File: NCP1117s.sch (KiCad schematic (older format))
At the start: 16 parts, among them U18 NCP1117ST33T3G, U19 AP2120N-1.8TRG1

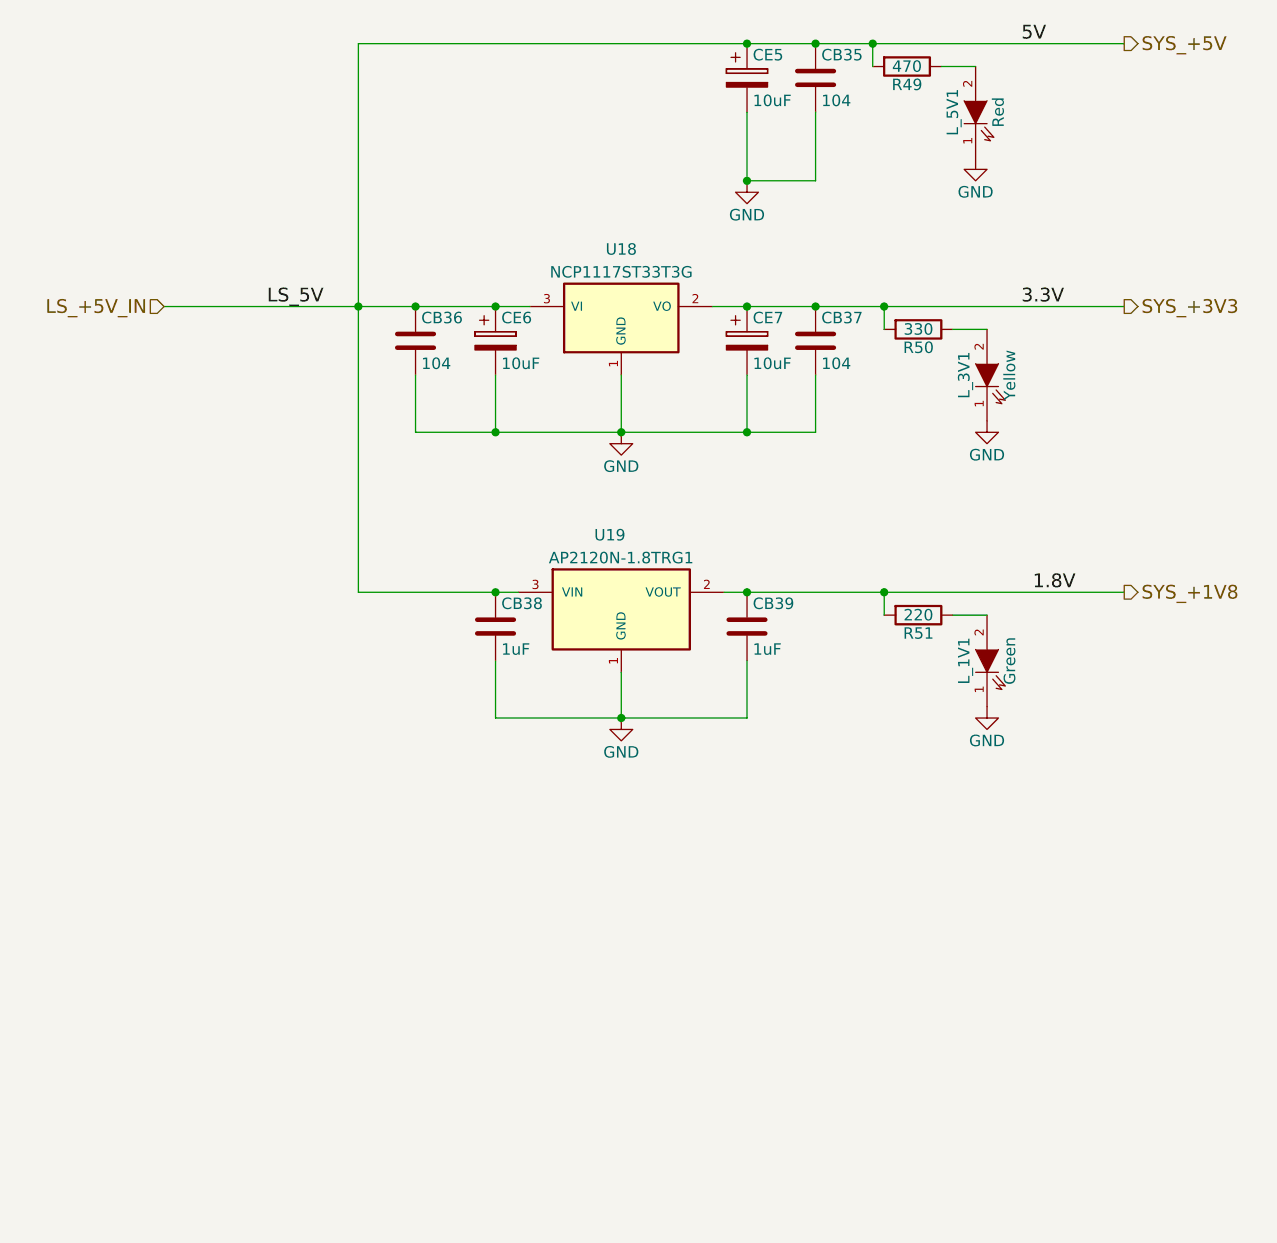
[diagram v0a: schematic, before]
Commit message: Improved the pin comatibility to match with other ardupilot project.
Signed-off-by: Akira Tsukamoto <akira-t@s9.dion.ne.jp>
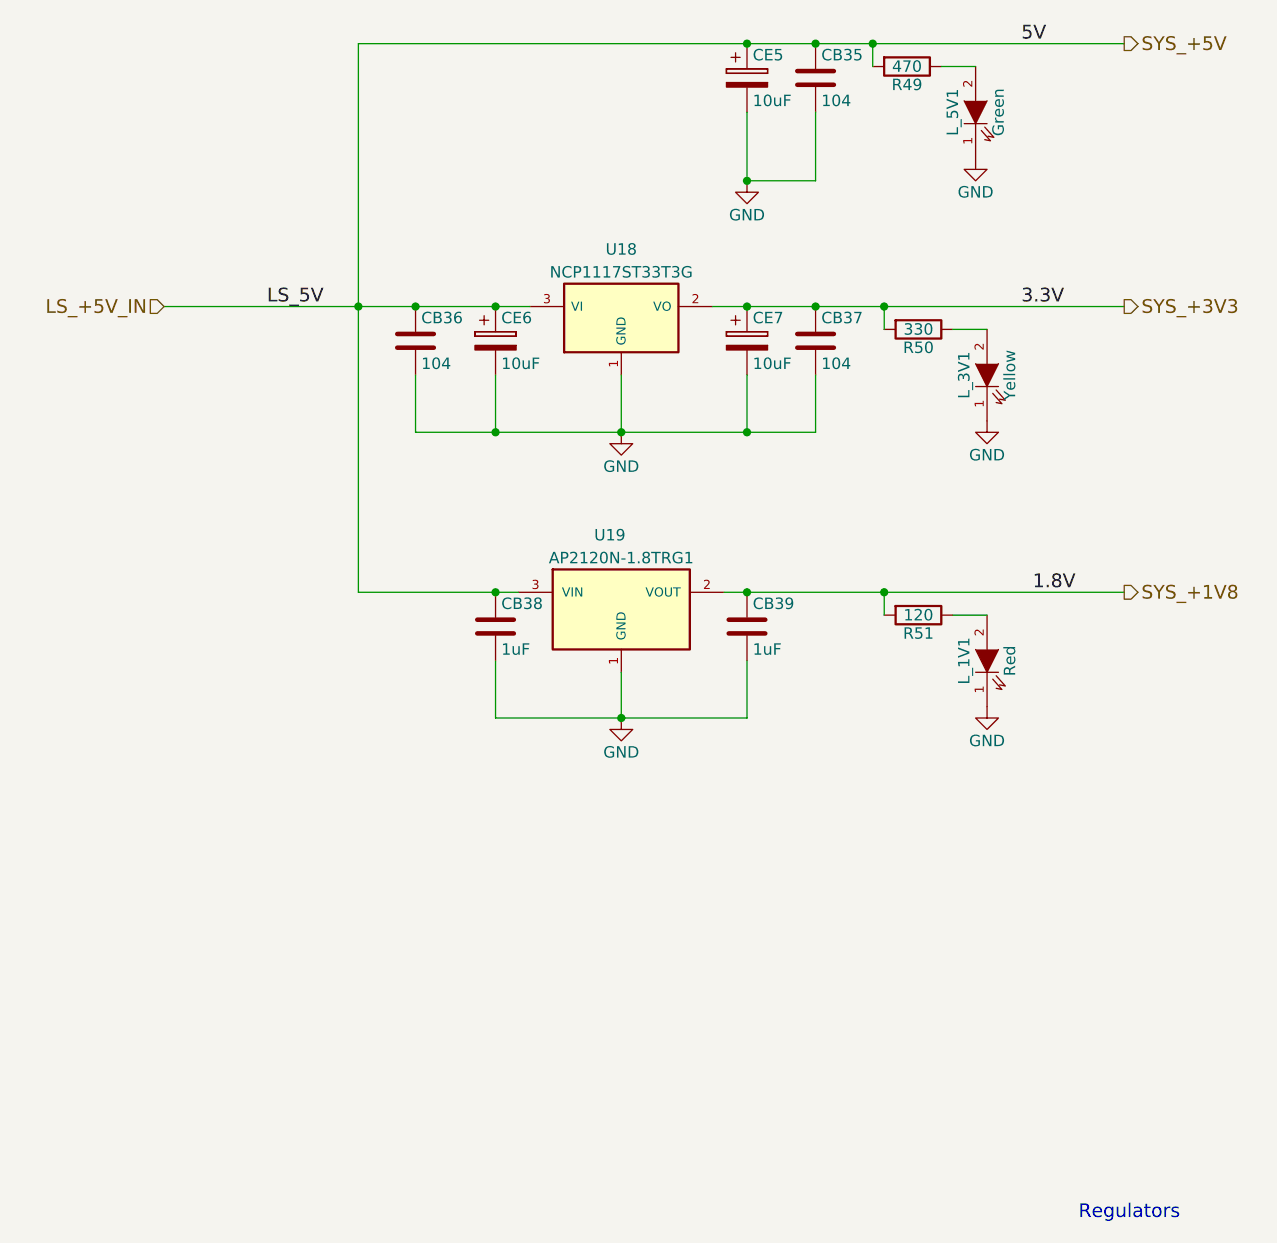
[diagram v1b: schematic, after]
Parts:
- L_1V1: value Green -> Red
- L_5V1: value Red -> Green
- R51: value 220 -> 120
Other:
- note added: "Regulators"
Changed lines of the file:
@@
 $EndDescr
 $Comp
-L GND #PWR094
+L GND #PWR096
 U 1 1 5707ADD4
 P 5300 4050
-F 0 "#PWR094" H 5300 3800 50  0001 C CNN
+F 0 "#PWR096" H 5300 3800 50  0001 C CNN
 F 1 "GND" H 5300 3900 50  0000 C CNN
 F 2 "" H 5300 4050 60  0000 C CNN
@@
 $EndComp
 $Comp
-L GND #PWR095
+L GND #PWR097
 U 1 1 5707AE00
 P 5300 5300
-F 0 "#PWR095" H 5300 5050 50  0001 C CNN
+F 0 "#PWR097" H 5300 5050 50  0001 C CNN
 F 1 "GND" H 5300 5150 50  0000 C CNN
 F 2 "" H 5300 5300 60  0000 C CNN
@@
 $EndComp
 $Comp
-L GND #PWR096
+L GND #PWR098
 U 1 1 5767AC24
 P 6900 4000
-F 0 "#PWR096" H 6900 3750 50  0001 C CNN
+F 0 "#PWR098" H 6900 3750 50  0001 C CNN
 F 1 "GND" H 6900 3850 50  0000 C CNN
 F 2 "" H 6900 4000 60  0000 C CNN
@@
 P 6600 4850
 F 0 "R51" V 6680 4850 50  0000 C CNN
-F 1 "220" V 6600 4850 50  0000 C CNN
+F 1 "120" V 6600 4850 50  0000 C CNN
 F 2 "droneworks:R_0603_Hand_droneworks" V 6530 4850 50  0001 C CNN
 F 3 "" H 6600 4850 50  0000 C CNN
@@
 P 6900 5050
 F 0 "L_1V1" H 6900 5150 50  0000 C CNN
-F 1 "Green" H 6900 4950 50  0000 C CNN
+F 1 "Red" H 6900 4950 50  0000 C CNN
 F 2 "droneworks:LED_0603_1608mm_droneworks" H 6900 5050 50  0001 C CNN
 F 3 "" H 6900 5050 50  0000 C CNN
@@
 $EndComp
 $Comp
-L GND #PWR097
+L GND #PWR099
 U 1 1 5767AE4A
 P 6900 5250
-F 0 "#PWR097" H 6900 5000 50  0001 C CNN
+F 0 "#PWR099" H 6900 5000 50  0001 C CNN
 F 1 "GND" H 6900 5100 50  0000 C CNN
 F 2 "" H 6900 5250 60  0000 C CNN
@@
 P 6850 2650
 F 0 "L_5V1" H 6850 2750 50  0000 C CNN
-F 1 "Red" H 6850 2550 50  0000 C CNN
+F 1 "Green" H 6850 2550 50  0000 C CNN
 F 2 "droneworks:LED_0603_1608mm_droneworks" H 6850 2650 50  0001 C CNN
 F 3 "" H 6850 2650 50  0000 C CNN
@@
 $EndComp
 $Comp
-L GND #PWR098
+L GND #PWR0100
 U 1 1 5767AF1B
 P 6850 2850
-F 0 "#PWR098" H 6850 2600 50  0001 C CNN
+F 0 "#PWR0100" H 6850 2600 50  0001 C CNN
 F 1 "GND" H 6850 2700 50  0000 C CNN
 F 2 "" H 6850 2850 60  0000 C CNN
@@
 $EndComp
 $Comp
-L GND #PWR099
+L GND #PWR0101
 U 1 1 58DB6F6B
 P 5850 2950
-F 0 "#PWR099" H 5850 2700 50  0001 C CNN
+F 0 "#PWR0101" H 5850 2700 50  0001 C CNN
 F 1 "GND" H 5850 2800 50  0000 C CNN
 F 2 "" H 5850 2950 60  0000 C CNN
@@
 Wire Wire Line
 	4150 4750 4850 4750
+Text Notes 7300 7500 0    60   ~ 0
+Regulators
 $EndSCHEMATC
